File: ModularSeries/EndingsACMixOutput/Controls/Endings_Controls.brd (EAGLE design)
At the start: 48.5 x 100 mm, 16 parts

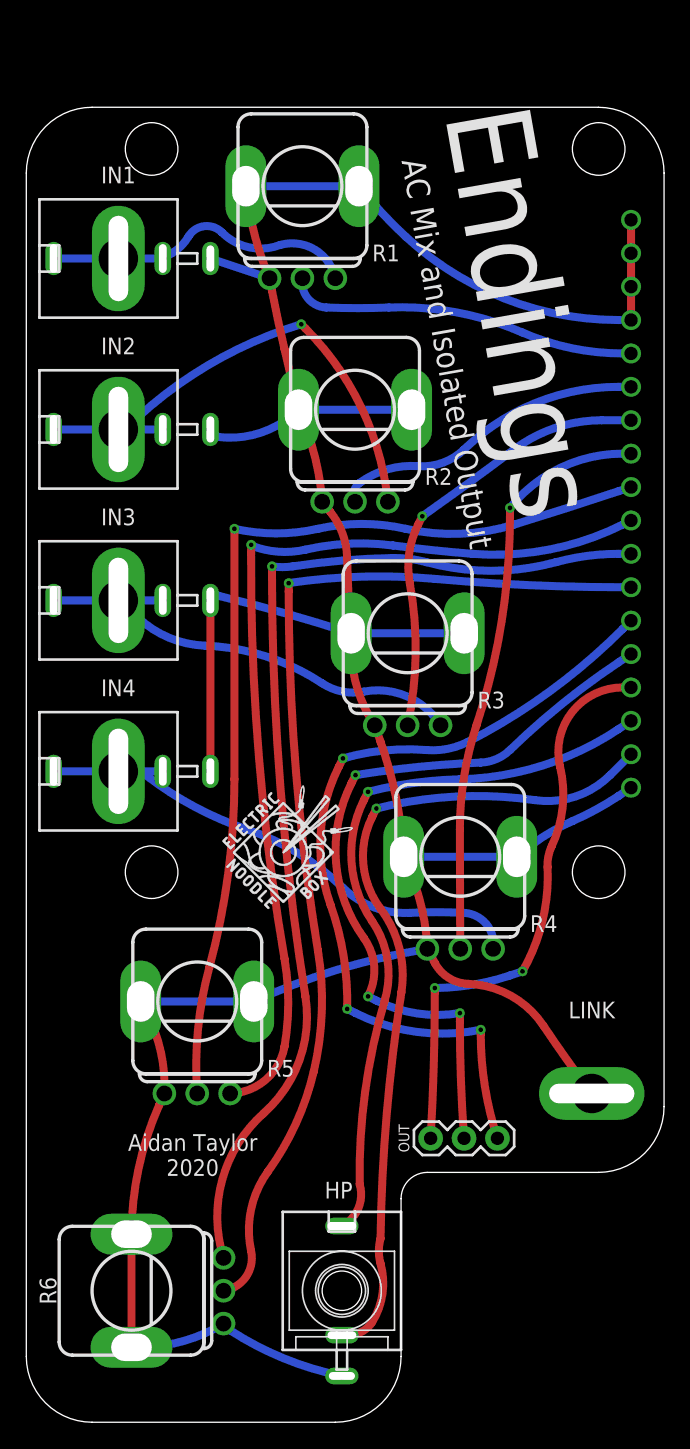
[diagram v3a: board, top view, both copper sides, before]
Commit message: Fields module images and BOM added
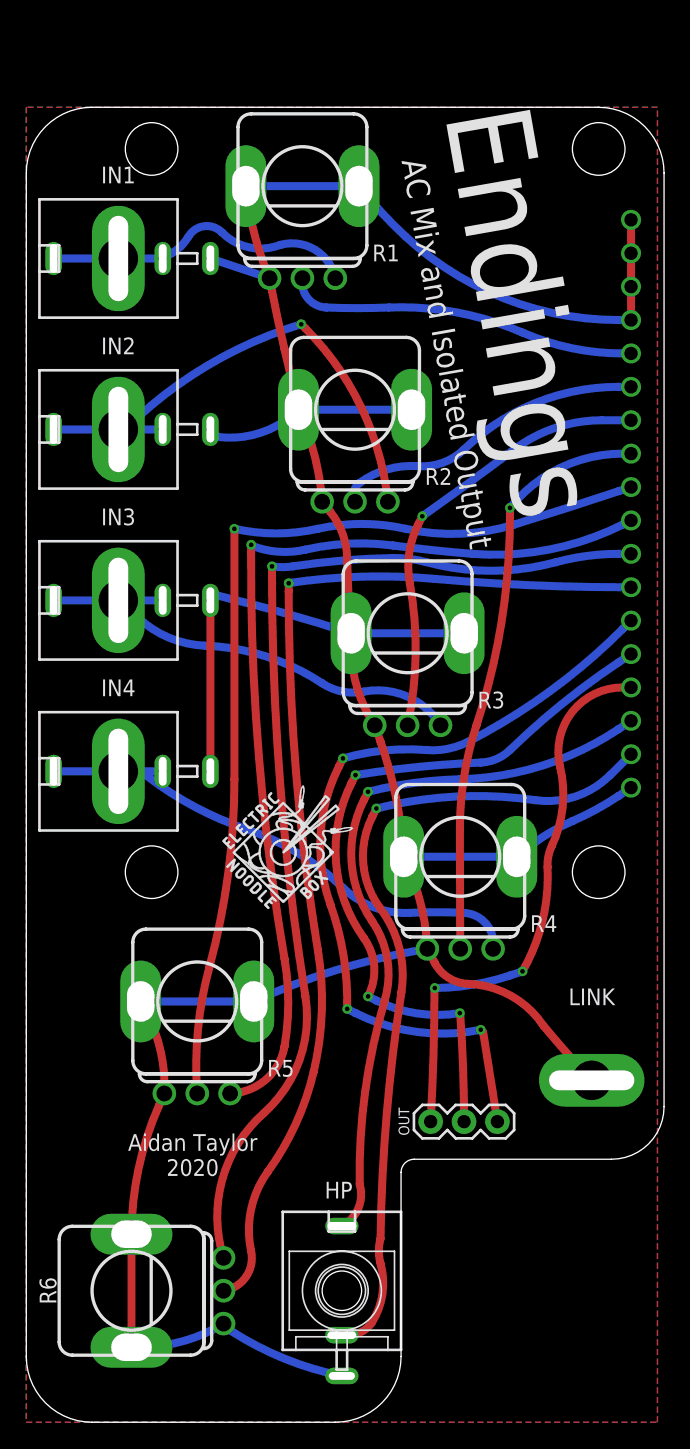
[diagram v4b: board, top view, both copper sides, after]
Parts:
- moved OUT 1.27 mm to (31.8, 22.9)
- moved LINK 1.00 mm to (44.0, 26.0)
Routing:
- net N$14: track 57.4 -> 56.1 mm
- net N$13: track 42.4 -> 41.1 mm
- net N$15: track 63.0 -> 61.8 mm
- net AGND: track 255.4 -> 254.6 mm
- added copper zone on layer 1, net AGND
- added copper zone on layer 16, net AGND
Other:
- outline, holes or cut-outs redrawn
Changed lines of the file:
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@@
 <setting verticaltext="up"/>
 </settings>
-<grid distance="12.5" unitdist="mil" unit="mil" style="lines" multiple="1" display="no" altdistance="5" altunitdist="mil" altunit="mil"/>
+<grid distance="1" unitdist="mm" unit="mm" style="lines" multiple="1" display="no" altdistance="5" altunitdist="mil" altunit="mil"/>
 <layers>
 <layer number="1" name="Top" color="4" fill="1" visible="yes" active="yes"/>
@@
 <text x="13.6525" y="20.32" size="1.27" layer="21" font="vector" ratio="16" align="center">Aidan Taylor
 2020</text>
-<wire x1="29.5" y1="5" x2="29.5" y2="17" width="0" layer="20"/>
-<wire x1="29.5" y1="17" x2="31.5" y2="19" width="0" layer="20" curve="-90"/>
-<wire x1="31.5" y1="19" x2="44.5" y2="19" width="0" layer="20"/>
-<wire x1="44.5" y1="19" x2="49.5" y2="24" width="0" layer="20" curve="90"/>
+<wire x1="29.5" y1="5" x2="29.5" y2="19" width="0" layer="20"/>
+<wire x1="29.5" y1="19" x2="30.5" y2="20" width="0" layer="20" curve="-90"/>
+<wire x1="30.5" y1="20" x2="45.5" y2="20" width="0" layer="20"/>
+<wire x1="45.5" y1="20" x2="49.5" y2="24" width="0" layer="20" curve="90"/>
 <wire x1="49.5" y1="24" x2="49.5" y2="95" width="0" layer="20"/>
 <wire x1="49.5" y1="95" x2="44.5" y2="100" width="0" layer="20" curve="90"/>
@@
 <elements>
 <element name="BOARD1" library="ElectricNoodleBox" package="ENDINGS" value="" x="49.53" y="36.83" smashed="yes" rot="MR0"/>
-<element name="LINK" library="ElectricNoodleBox" package="CINCHNANA_PANEL" value="BANANA_PANEL" x="44" y="25" smashed="yes">
-<attribute name="NAME" x="44" y="31.35" size="1.27" layer="25" font="vector" align="center"/>
+<element name="LINK" library="ElectricNoodleBox" package="CINCHNANA_PANEL" value="BANANA_PANEL" x="44" y="26" smashed="yes">
+<attribute name="NAME" x="44" y="32.35" size="1.27" layer="25" font="vector" align="center"/>
 </element>
 <element name="R1" library="ElectricNoodleBox" package="ALPHA_RV09_9MMPOT" value="B100K" x="22" y="94" smashed="yes">
@@
 <attribute name="VALUE" x="16.62" y="17.62" size="1.27" layer="27" rot="R90" align="center"/>
 </element>
-<element name="OUT" library="ElectricNoodleBox" package="1X03" value="3XWIREPAD" x="31.75" y="21.59" smashed="yes">
-<attribute name="NAME" x="29.718" y="21.59" size="0.8128" layer="25" font="vector" ratio="20" rot="R90" align="center"/>
-<attribute name="VALUE" x="32.385" y="23.368" size="0.6096" layer="27" font="vector" ratio="20"/>
+<element name="OUT" library="ElectricNoodleBox" package="1X03" value="3XWIREPAD" x="31.75" y="22.86" smashed="yes">
+<attribute name="NAME" x="29.718" y="22.86" size="0.8128" layer="25" font="vector" ratio="20" rot="R90" align="center"/>
+<attribute name="VALUE" x="32.385" y="24.638" size="0.6096" layer="27" font="vector" ratio="20"/>
 </element>
 <element name="HP" library="ElectricNoodleBox" package="STEREO_JACK_PANEL" value="STEREOJACK" x="25" y="10" smashed="yes">
@@
 <wire x1="32.0675" y1="34.925" x2="34.6075" y2="33.3375" width="0.6096" layer="1" curve="60.329462"/>
 <wire x1="34.6075" y1="33.3375" x2="40.3225" y2="30.1625" width="0.6096" layer="1" curve="-54.427892"/>
-<wire x1="40.3225" y1="30.1625" x2="44" y2="25" width="0.6096" layer="1" curve="3.465314"/>
+<wire x1="40.3225" y1="30.1625" x2="44" y2="26" width="0.6096" layer="1" curve="3.465314"/>
 <wire x1="21.7" y1="77" x2="30.3" y2="77" width="0.6096" layer="16"/>
+<polygon width="0.5" layer="1">
+<vertex x="1" y="0"/>
+<vertex x="49" y="0"/>
+<vertex x="49" y="100"/>
+<vertex x="1" y="100"/>
+</polygon>
+<polygon width="0.5" layer="16">
+<vertex x="1" y="0"/>
+<vertex x="49" y="0"/>
+<vertex x="49" y="100"/>
+<vertex x="1" y="100"/>
+</polygon>
 </signal>
 <signal name="N$1">
@@
 <wire x1="37.7825" y1="33.9725" x2="32.0675" y2="33.02" width="0.6096" layer="16" curve="-17.945253"/>
 <via x="32.0675" y="33.02" extent="1-16" drill="0.35"/>
-<wire x1="32.0675" y1="33.02" x2="32.0675" y2="32.7025" width="0.6096" layer="1"/>
-<wire x1="32.0675" y1="32.7025" x2="31.75" y2="21.59" width="0.6096" layer="1" curve="-3.273154"/>
+<wire x1="32.0675" y1="33.02" x2="32.039484375" y2="32.991984375" width="0.6096" layer="1"/>
+<wire x1="32.039484375" y1="32.991984375" x2="31.75" y2="22.86" width="0.6096" layer="1" curve="-3.273154"/>
 </signal>
 <signal name="N$15">
@@
 <wire x1="26.035" y1="31.115" x2="35.56" y2="29.845" width="0.6096" layer="16" curve="37.940812"/>
 <via x="35.56" y="29.845" extent="1-16" drill="0.35"/>
-<wire x1="35.56" y1="29.845" x2="35.56" y2="29.5275" width="0.6096" layer="1"/>
-<wire x1="35.56" y1="29.5275" x2="36.83" y2="21.59" width="0.6096" layer="1" curve="18.180554"/>
+<wire x1="36.83" y1="22.86" x2="35.741428125" y2="29.663571875" width="0.6096" layer="1"/>
+<wire x1="35.56" y1="29.845" x2="35.741428125" y2="29.663571875" width="0.6096" layer="1" curve="18.180554"/>
 </signal>
 <signal name="N$16">
@@
 <wire x1="27.6225" y1="32.0675" x2="33.9725" y2="31.115" width="0.6096" layer="16" curve="36.068575"/>
 <via x="33.9725" y="31.115" extent="1-16" drill="0.35"/>
-<wire x1="33.9725" y1="31.115" x2="33.9725" y2="30.48" width="0.6096" layer="1"/>
-<wire x1="33.9725" y1="30.48" x2="34.29" y2="21.59" width="0.6096" layer="1" curve="4.090817"/>
+<wire x1="33.9725" y1="31.115" x2="33.99601875" y2="31.09148125" width="0.6096" layer="1"/>
+<wire x1="34.29" y1="22.86" x2="33.99601875" y2="31.09148125" width="0.6096" layer="1" curve="4.090817"/>
 </signal>
 <signal name="N$11">
